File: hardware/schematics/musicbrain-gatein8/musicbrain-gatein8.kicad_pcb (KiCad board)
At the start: 2 copper layers, 40 x 80 mm, 32 parts, among them J1 BUS, J2 GATES IN, U1 74HC165, U2 74LVC1G125

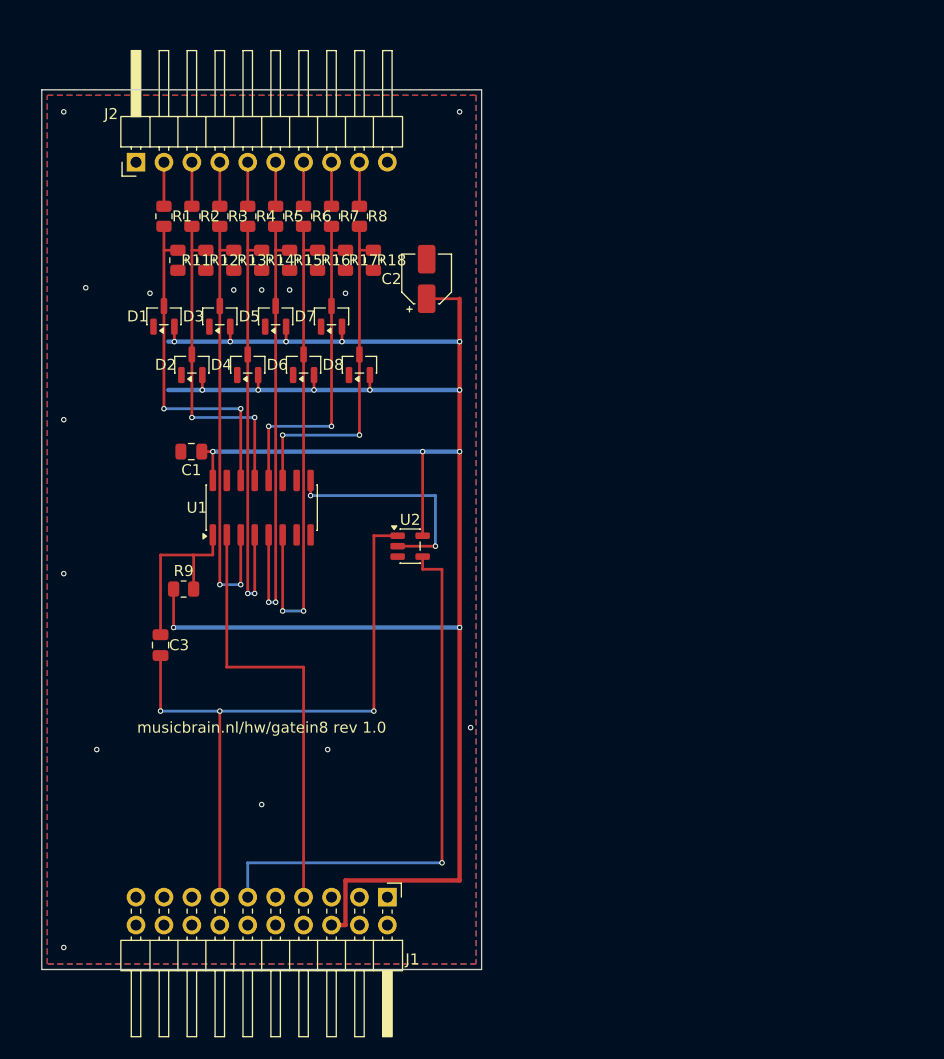
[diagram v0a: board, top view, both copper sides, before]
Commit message: gatein8 gen 2: 80x45, slot 2x12, freerouting
- kaart 40x80 -> 80x45 (bus.KAART_B x bus.H); J1 2x10 -> 2x12 via bus.j1_map
- J2 1x10 gecentreerd op het kaarthart, paneelinzet 4,04
- kanaal-conditionering (100k/100k/BAT54S) in kolommen onder de J2-pinnen;
  D_OF_IN-mapping ongewijzigd (firmware-contract)
- handroutes vervangen door freerouting-SES + gnd_stitch.json
- ERC 0, netcheck OK, DRC 0/0

Co-Authored-By: Claude Fable 5 <noreply@anthropic.com>
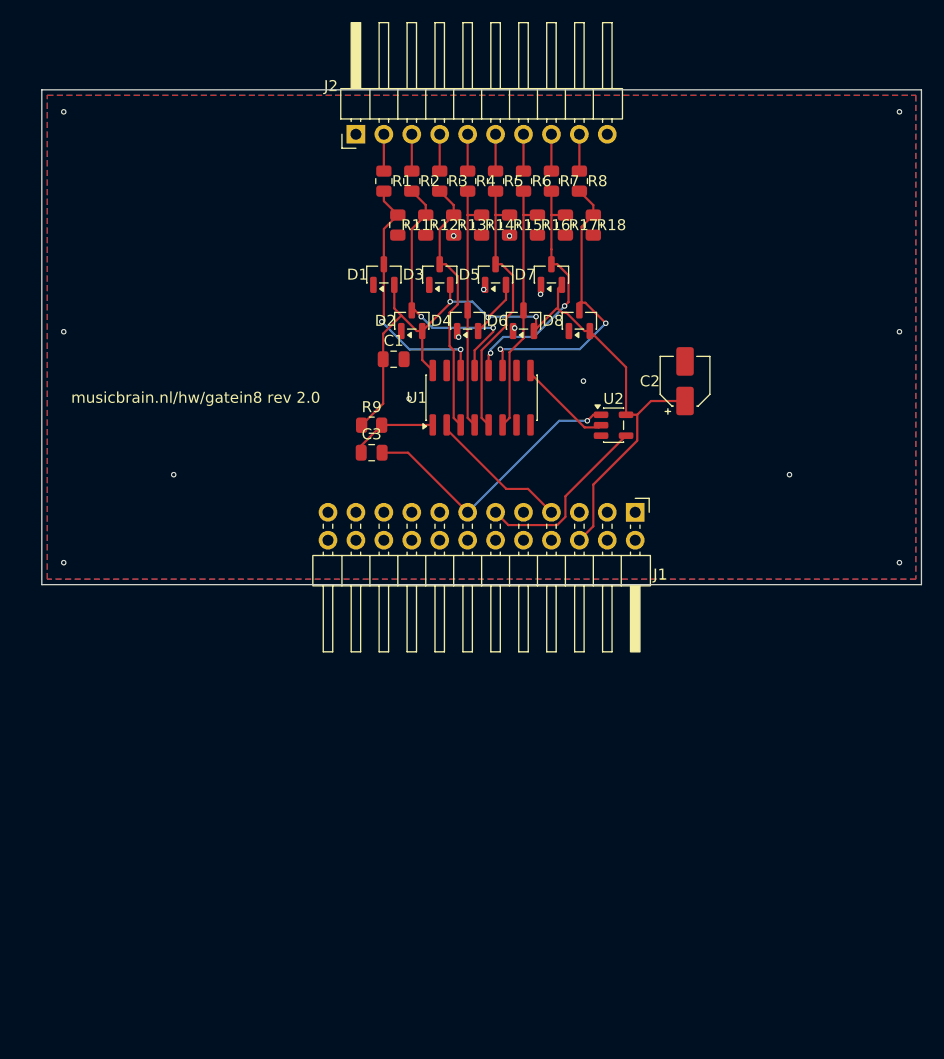
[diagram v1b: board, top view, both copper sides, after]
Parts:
- D1: renamed from R1; value 100k -> BAT54S; footprint Resistor_SMD:R_0805_2012Metric -> Package_TO_SOT_SMD:SOT-23
- D2: renamed from R2; value 100k -> BAT54S; footprint Resistor_SMD:R_0805_2012Metric -> Package_TO_SOT_SMD:SOT-23
- D3: renamed from R3; value 100k -> BAT54S; footprint Resistor_SMD:R_0805_2012Metric -> Package_TO_SOT_SMD:SOT-23
- D4: renamed from R4; value 100k -> BAT54S; footprint Resistor_SMD:R_0805_2012Metric -> Package_TO_SOT_SMD:SOT-23
- D5: renamed from R5; value 100k -> BAT54S; footprint Resistor_SMD:R_0805_2012Metric -> Package_TO_SOT_SMD:SOT-23
- D6: renamed from R6; value 100k -> BAT54S; footprint Resistor_SMD:R_0805_2012Metric -> Package_TO_SOT_SMD:SOT-23
- D7: renamed from R7; value 100k -> BAT54S; footprint Resistor_SMD:R_0805_2012Metric -> Package_TO_SOT_SMD:SOT-23
- D8: renamed from R8; value 100k -> BAT54S; footprint Resistor_SMD:R_0805_2012Metric -> Package_TO_SOT_SMD:SOT-23
- J1: footprint Connector_PinHeader_2.54mm:PinHeader_2x10_P2.54mm_Horizontal -> Connector_PinHeader_2.54mm:PinHeader_2x12_P2.54mm_Horizontal
- R1: renamed from U1; value 74HC165 -> 100k; footprint Package_SO:SOIC-16_3.9x9.9mm_P1.27mm -> Resistor_SMD:R_0805_2012Metric
- R11: renamed from U2; value 74LVC1G125 -> 100k; footprint Package_TO_SOT_SMD:SOT-23-5 -> Resistor_SMD:R_0805_2012Metric
- R12: renamed from D1; value BAT54S -> 100k; footprint Package_TO_SOT_SMD:SOT-23 -> Resistor_SMD:R_0805_2012Metric
- R13: renamed from D2; value BAT54S -> 100k; footprint Package_TO_SOT_SMD:SOT-23 -> Resistor_SMD:R_0805_2012Metric
- R14: renamed from D3; value BAT54S -> 100k; footprint Package_TO_SOT_SMD:SOT-23 -> Resistor_SMD:R_0805_2012Metric
- R15: renamed from D4; value BAT54S -> 100k; footprint Package_TO_SOT_SMD:SOT-23 -> Resistor_SMD:R_0805_2012Metric
- R16: renamed from D5; value BAT54S -> 100k; footprint Package_TO_SOT_SMD:SOT-23 -> Resistor_SMD:R_0805_2012Metric
- R17: renamed from D6; value BAT54S -> 100k; footprint Package_TO_SOT_SMD:SOT-23 -> Resistor_SMD:R_0805_2012Metric
- R18: renamed from D7; value BAT54S -> 100k; footprint Package_TO_SOT_SMD:SOT-23 -> Resistor_SMD:R_0805_2012Metric
- U1: renamed from R18; value 100k -> 74HC165; footprint Resistor_SMD:R_0805_2012Metric -> Package_SO:SOIC-16_3.9x9.9mm_P1.27mm
- U2: renamed from D8; value BAT54S -> 74LVC1G125; footprint Package_TO_SOT_SMD:SOT-23 -> Package_TO_SOT_SMD:SOT-23-5
- moved J1 41.6 mm to (154.0, 138.4)
- moved R1 31.7 mm to (131.1, 108.3), turned to 270 degrees
- moved R11 29.2 mm to (132.4, 112.3), turned to 270 degrees
- moved R13 27.0 mm to (137.5, 112.3), turned to 270 degrees
- moved R17 27.0 mm to (147.6, 112.3), turned to 270 degrees
- moved R15 27.0 mm to (142.5, 112.3), turned to 270 degrees
- moved C3 26.0 mm to (130.0, 133.0), turned to 0 degrees
- moved C2 25.3 mm to (158.5, 126.5)
- moved R16 25.2 mm to (145.1, 112.3), turned to 270 degrees
- moved R14 25.2 mm to (140.0, 112.3), turned to 270 degrees
- moved R18 25.2 mm to (150.2, 112.3), turned to 270 degrees
- moved R12 25.2 mm to (134.9, 112.3), turned to 270 degrees
- moved U2 23.8 mm to (152.0, 130.5), turned to 0 degrees
- moved R9 22.7 mm to (130.0, 130.5)
- moved R2 22.5 mm to (133.7, 108.3)
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- renumbered R11 to R2, R12 to R3, R13 to R4, R14 to R5, R15 to R6, R16 to R7, R17 to R8
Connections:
- D1 pad 1: /IN1 -> GND
- D1 pad 2: /N1 -> +3V3
- D2 pad 1: /IN2 -> GND
- D2 pad 2: /N2 -> +3V3
- D3 pad 1: /IN3 -> GND
- D3 pad 2: /N3 -> +3V3
- D4 pad 1: /IN4 -> GND
- D4 pad 2: /N4 -> +3V3
- D5 pad 1: /IN5 -> GND
- D5 pad 2: /N5 -> +3V3
- D6 pad 1: /IN6 -> GND
- D6 pad 2: /N6 -> +3V3
- D7 pad 1: /IN7 -> GND
- D7 pad 2: /N7 -> +3V3
- D8 pad 1: /IN8 -> GND
- D8 pad 2: /N8 -> +3V3
- J1 pad 20: (no net) -> GND
- R1 pad 1: /PL -> /IN1
- R1 pad 2: /SCLK -> /N1
- R11 pad 1: /CS -> /N1
- R11 pad 2: /Q7 -> GND
- R12 pad 1: GND -> /N2
- R12 pad 2: +3V3 -> GND
- R13 pad 1: GND -> /N3
- R13 pad 2: +3V3 -> GND
- R14 pad 1: GND -> /N4
- R14 pad 2: +3V3 -> GND
- R15 pad 1: GND -> /N5
- R15 pad 2: +3V3 -> GND
- R16 pad 1: GND -> /N6
- R16 pad 2: +3V3 -> GND
- R17 pad 1: GND -> /N7
- R17 pad 2: +3V3 -> GND
- R18 pad 1: GND -> /N8
- R18 pad 2: +3V3 -> GND
- R2 pad 1: /N1 -> /IN2
- R2 pad 2: GND -> /N2
- R3 pad 1: /N2 -> /IN3
- R3 pad 2: GND -> /N3
- R4 pad 1: /N3 -> /IN4
- R4 pad 2: GND -> /N4
- R5 pad 1: /N4 -> /IN5
- R5 pad 2: GND -> /N5
- R6 pad 1: /N5 -> /IN6
- R6 pad 2: GND -> /N6
- R7 pad 1: /N6 -> /IN7
- R7 pad 2: GND -> /N7
- R8 pad 1: /N7 -> /IN8
- R8 pad 2: GND -> /N8
- U1 pad 1: /N8 -> /PL
- U1 pad 2: GND -> /SCLK
- U2 pad 1: GND -> /CS
- U2 pad 2: +3V3 -> /Q7
- U2 pad 3: /N8 -> GND
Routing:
- net +3V3: track 198.7 -> 78.9 mm, vias 15 -> 3
- net /CS: track 59.5 -> 25.8 mm, vias 3 -> 1
- net /MISO: track 50.4 -> 16.8 mm, vias 1 -> 0
- net /SCLK: track 39.9 -> 13.0 mm
- net /N6: track 45.1 -> 23.3 mm, vias 2 -> 0
- net /N4: track 40.6 -> 22.8 mm, vias 2 -> 0
- net /N5: track 42.2 -> 25.0 mm, vias 2 -> 0
- net /N3: track 40.3 -> 24.0 mm, vias 2 -> 0
- net /Q7: track 20.8 -> 8.79 mm, vias 2 -> 0
- net /PL: track 16.9 -> 7.92 mm
- net /N1: track 31.4 -> 23.1 mm
- net /N7: track 30.1 -> 23.2 mm
- net /N2: track 30.1 -> 24.5 mm
- net /N8: track 31.4 -> 28.0 mm
- net /IN8: track 4.01 -> 3.35 mm
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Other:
- board size 40 x 80 mm -> 80 x 45 mm
- board text added: "musicbrain.nl/hw/gatein8 rev 2.0"
- board text removed: "musicbrain.nl/hw/gatein8 rev 1.0"

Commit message: afslank-ronde: potriser 40, gatein8 50, gate8 55, dac8 60, adc8 65 (x45)
80 mm was een maximum, geen eis (observatie Mark): J1/J2 blijven op de
hartlijn, de rand schuift naar binnen. Silk verticaal in de westrand
(horizontaal paste niet meer); hoekvia's geparametriseerd op BX0/BX1;
zwervers mee (gate8 C1, dac8 C3, adc8 JP1). Alle vijf opnieuw geroute
(verse SES) en op ERC 0 + netcheck OK + DRC 0/0.

Co-Authored-By: Claude Fable 5 <noreply@anthropic.com>
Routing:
- net +3V3: track 78.9 -> 102.9 mm
- net /N6: track 23.3 -> 32.9 mm, vias 0 -> 2
- net /CS: track 25.8 -> 35.4 mm, vias 1 -> 0
- net /N2: track 24.5 -> 33.5 mm
- net /MISO: track 16.8 -> 22.4 mm
- net /SCLK: track 13.0 -> 17.8 mm, vias 0 -> 1
- net /N7: track 23.2 -> 20.4 mm
- net /N8: track 28.0 -> 25.3 mm
- net /N1: track 23.1 -> 21.5 mm, vias 2 -> 0
- net /N3: track 24.0 -> 25.0 mm
- net /N5: track 25.0 -> 24.2 mm
- net /N4: track 22.8 -> 23.3 mm
- net GND: vias 16 -> 17
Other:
- board size 80 x 45 mm -> 50 x 45 mm
